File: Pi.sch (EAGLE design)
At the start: 11 parts, among them X1 RASPI_GPIO_B+#_BOX, X2 HDD, 5V 700mA, X3 MAC64L

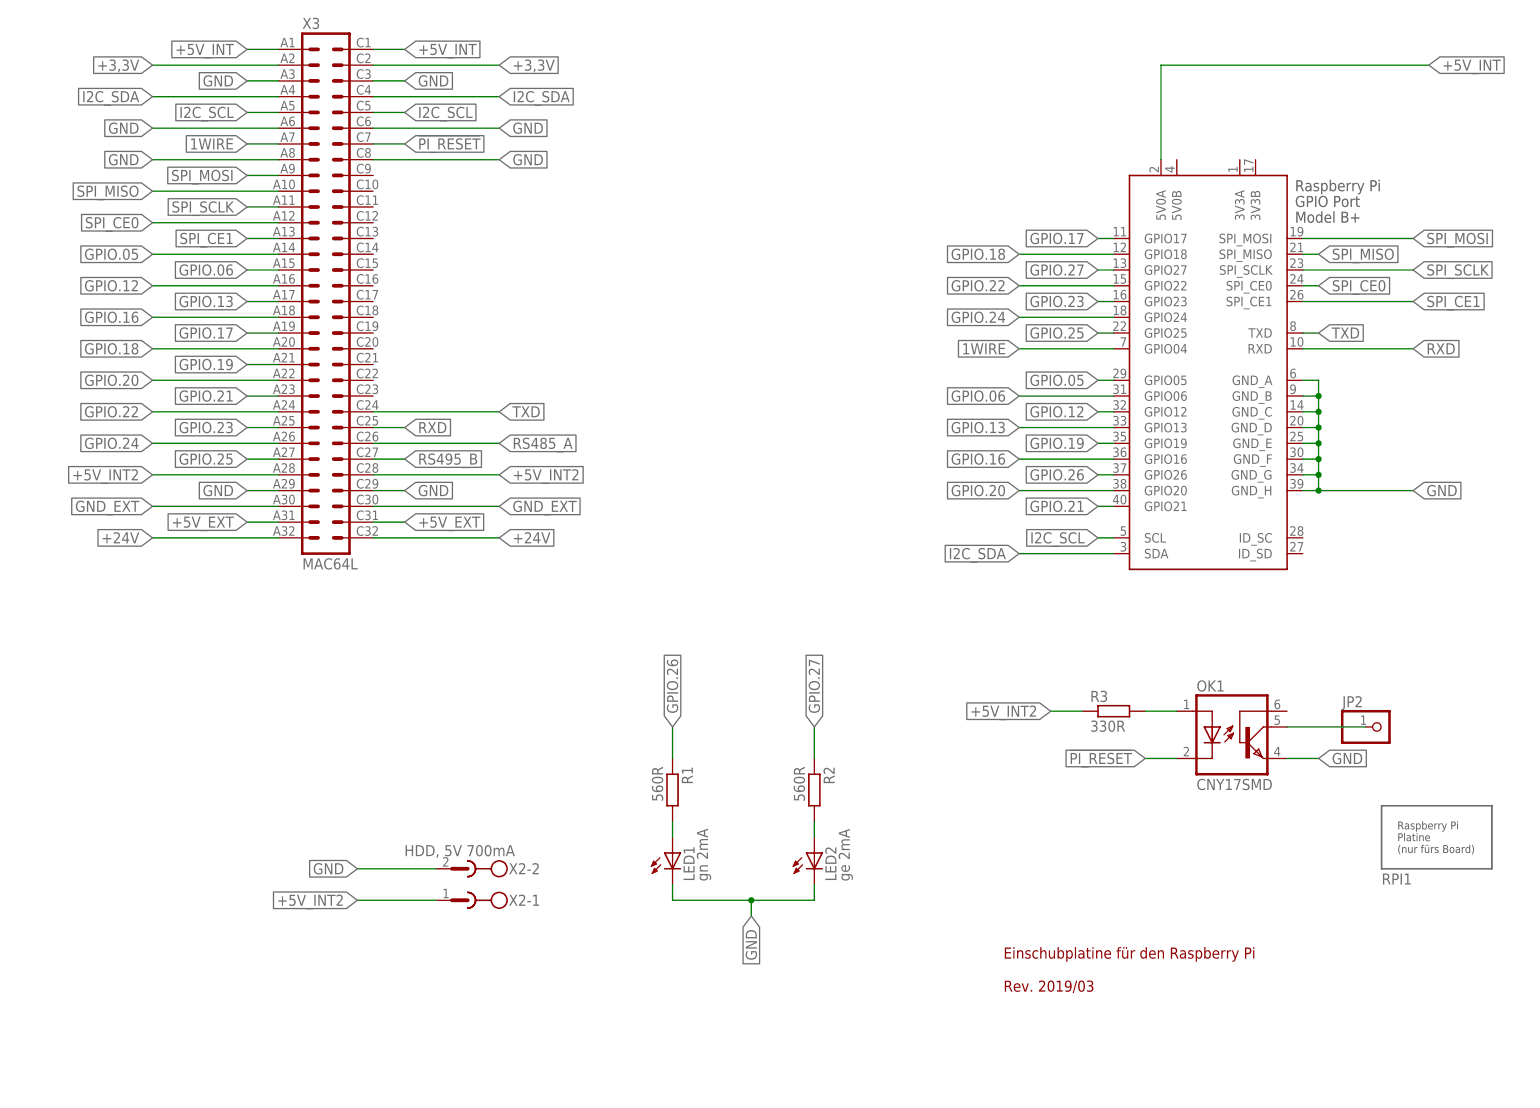
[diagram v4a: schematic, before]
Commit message: 1-Wire Sensor auf Raspi-Platine
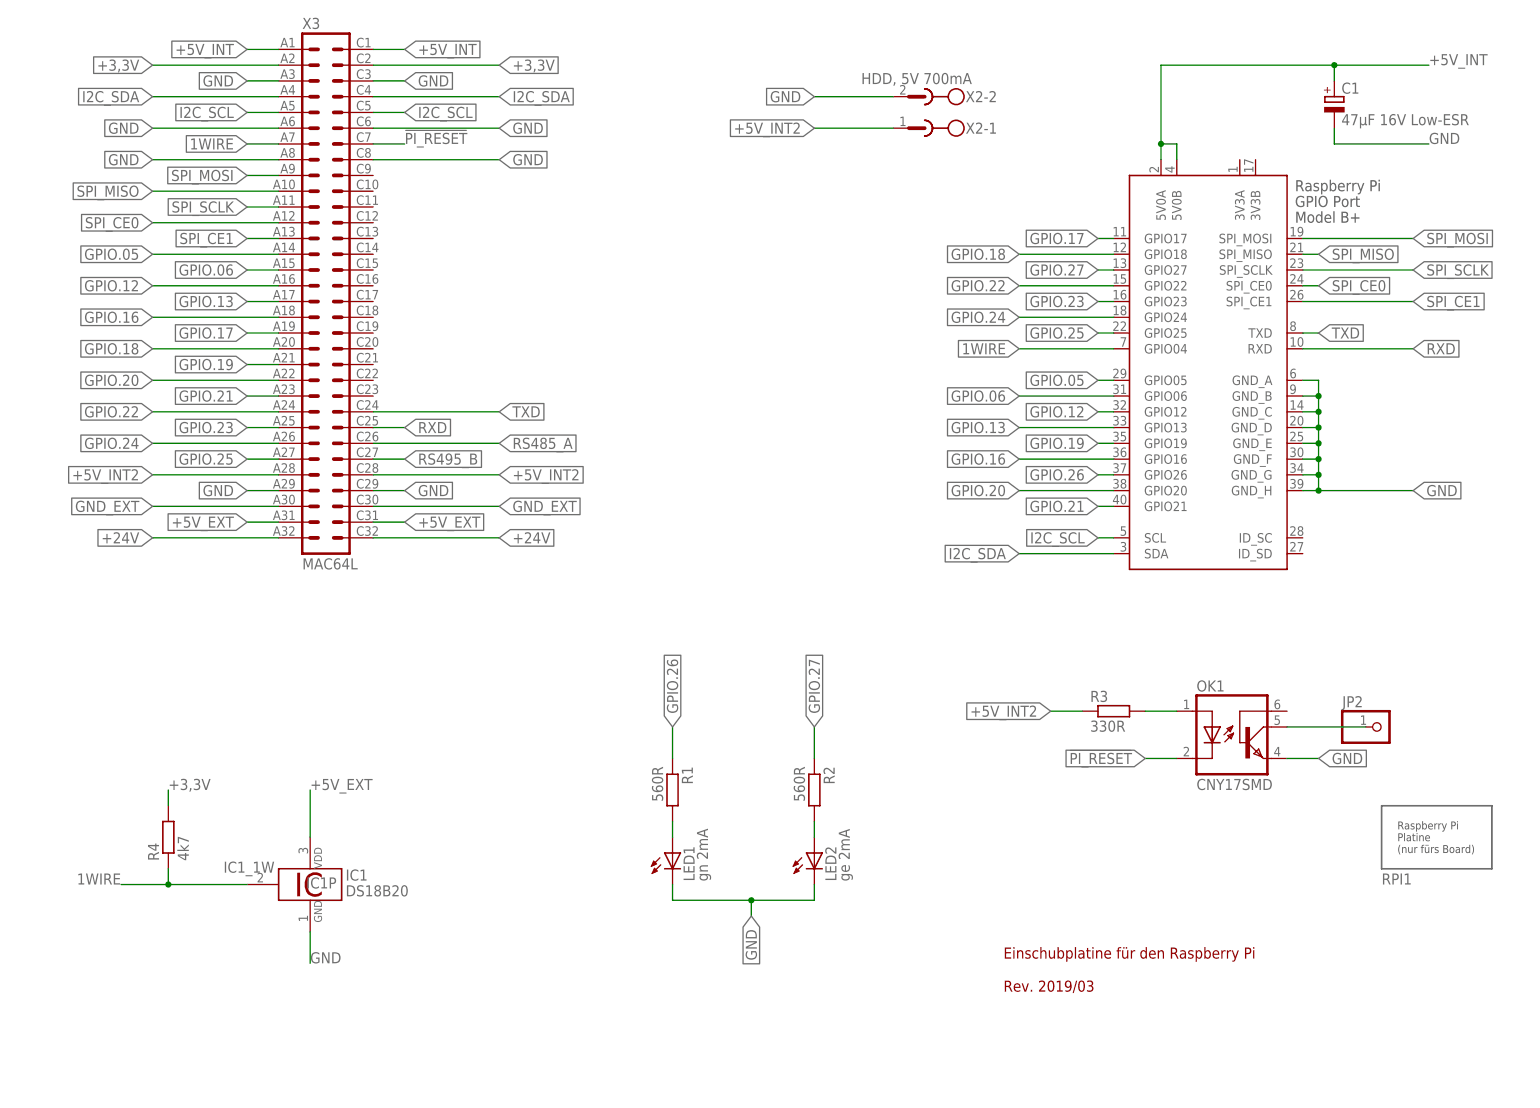
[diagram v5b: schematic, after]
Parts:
- added C1: 47µF 16V Low-ESR, rcl:CPOL-EUE2-5
- added IC1: DS18B20, 1wire:DS18B20
- added R4: 4k7, rcl:R-EU_0204/7
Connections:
- net +3,3V: now also R4.2
- net +5V_EXT: now also IC1P.VDD
- net +5V_INT: now also C1.+, X1.5V0B
- net 1WIRE: now also IC1_1W.1W, R4.1
- net GND: now also C1.-, IC1P.GND
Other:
- moved on the sheet: X2-1, X2-2
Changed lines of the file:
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@@
 <layer number="48" name="Document" color="7" fill="1" visible="no" active="no"/>
 <layer number="49" name="Reference" color="7" fill="1" visible="no" active="no"/>
+<layer number="50" name="dxf" color="7" fill="1" visible="no" active="no"/>
 <layer number="51" name="tDocu" color="7" fill="1" visible="no" active="no"/>
 <layer number="52" name="bDocu" color="7" fill="1" visible="no" active="no"/>
@@
 <layer number="98" name="Guide" color="6" fill="1" visible="yes" active="yes"/>
 <layer number="99" name="SpiceOrder" color="5" fill="1" visible="yes" active="yes"/>
+<layer number="250" name="Descript" color="3" fill="1" visible="no" active="no"/>
+<layer number="251" name="SMDround" color="12" fill="11" visible="no" active="no"/>
 </layers>
 <schematic xreflabel="%F%N/%S.%C%R" xrefpart="/%S.%C%R">
@@
 <part name="OK1" library="homepi" deviceset="CNY17" device="SMD"/>
 <part name="R3" library="rcl" deviceset="R-EU_" device="0204/5" value="330R"/>
+<part name="C1" library="rcl" deviceset="CPOL-EU" device="E2-5" value="47µF 16V Low-ESR"/>
+<part name="IC1" library="1wire" deviceset="DS18B20" device=""/>
+<part name="R4" library="rcl" deviceset="R-EU_" device="0204/7" value="4k7"/>
 </parts>
 <sheets>
@@
 <instance part="R2" gate="G$1" x="132.08" y="45.72" rot="R270"/>
 <instance part="LED2" gate="G$1" x="132.08" y="35.56"/>
-<instance part="X2" gate="-1" x="76.2" y="27.94" rot="R180"/>
-<instance part="X2" gate="-2" x="76.2" y="33.02" rot="R180"/>
+<instance part="X2" gate="-1" x="149.86" y="152.4" rot="R180"/>
+<instance part="X2" gate="-2" x="149.86" y="157.48" rot="R180"/>
 <instance part="X3" gate="G$1" x="53.34" y="127"/>
 <instance part="JP2" gate="G$1" x="223.52" y="55.88"/>
@@
 <instance part="OK1" gate="G$1" x="200.66" y="55.88"/>
 <instance part="R3" gate="G$1" x="180.34" y="58.42"/>
+<instance part="C1" gate="G$1" x="215.9" y="157.48"/>
+<instance part="IC1" gate="A" x="50.8" y="30.48"/>
+<instance part="IC1" gate="P" x="50.8" y="30.48"/>
+<instance part="IC1" gate="_1W" x="45.72" y="30.48"/>
+<instance part="R4" gate="G$1" x="27.94" y="38.1" rot="R90"/>
 </instances>
 <busses>
@@
 <label x="40.64" y="149.86" size="1.778" layer="95" rot="R180" xref="yes"/>
 </segment>
+<segment>
+<pinref part="IC1" gate="_1W" pin="1W"/>
+<wire x1="40.64" y1="30.48" x2="27.94" y2="30.48" width="0.1524" layer="91"/>
+<label x="20.32" y="30.48" size="1.778" layer="95" rot="MR0"/>
+<pinref part="R4" gate="G$1" pin="1"/>
+<wire x1="27.94" y1="30.48" x2="20.32" y2="30.48" width="0.1524" layer="91"/>
+<wire x1="27.94" y1="30.48" x2="27.94" y2="33.02" width="0.1524" layer="91"/>
+<junction x="27.94" y="30.48"/>
+</segment>
 </net>
 <net name="SPI_MOSI" class="0">
@@
 <label x="81.28" y="162.56" size="1.778" layer="95" xref="yes"/>
 </segment>
+<segment>
+<pinref part="R4" gate="G$1" pin="2"/>
+<wire x1="27.94" y1="43.18" x2="27.94" y2="45.72" width="0.1524" layer="91"/>
+<label x="27.94" y="45.72" size="1.778" layer="95"/>
+</segment>
 </net>
 <net name="N$15" class="0">
@@
 <segment>
 <pinref part="X2" gate="-1" pin="1"/>
-<wire x1="58.42" y1="27.94" x2="71.12" y2="27.94" width="0.1524" layer="91"/>
-<label x="58.42" y="27.94" size="1.778" layer="95" rot="R180" xref="yes"/>
+<wire x1="132.08" y1="152.4" x2="144.78" y2="152.4" width="0.1524" layer="91"/>
+<label x="132.08" y="152.4" size="1.778" layer="95" rot="R180" xref="yes"/>
 </segment>
 <segment>
@@
 <segment>
 <pinref part="X1" gate="G$1" pin="5V0A"/>
-<wire x1="187.96" y1="147.32" x2="187.96" y2="162.56" width="0.1524" layer="91"/>
-<wire x1="187.96" y1="162.56" x2="231.14" y2="162.56" width="0.1524" layer="91"/>
-<label x="231.14" y="162.56" size="1.778" layer="95" xref="yes"/>
+<wire x1="187.96" y1="147.32" x2="187.96" y2="149.86" width="0.1524" layer="91"/>
+<wire x1="187.96" y1="149.86" x2="187.96" y2="162.56" width="0.1524" layer="91"/>
+<wire x1="187.96" y1="162.56" x2="215.9" y2="162.56" width="0.1524" layer="91"/>
+<label x="231.14" y="162.56" size="1.778" layer="95"/>
+<pinref part="C1" gate="G$1" pin="+"/>
+<wire x1="215.9" y1="162.56" x2="231.14" y2="162.56" width="0.1524" layer="91"/>
+<wire x1="215.9" y1="160.02" x2="215.9" y2="162.56" width="0.1524" layer="91"/>
+<junction x="215.9" y="162.56"/>
+<pinref part="X1" gate="G$1" pin="5V0B"/>
+<wire x1="187.96" y1="149.86" x2="190.5" y2="149.86" width="0.1524" layer="91"/>
+<wire x1="190.5" y1="149.86" x2="190.5" y2="147.32" width="0.1524" layer="91"/>
+<junction x="187.96" y="149.86"/>
 </segment>
 <segment>
@@
 <label x="66.04" y="88.9" size="1.778" layer="95" xref="yes"/>
 </segment>
+<segment>
+<pinref part="IC1" gate="P" pin="VDD"/>
+<wire x1="50.8" y1="45.72" x2="50.8" y2="38.1" width="0.1524" layer="91"/>
+<label x="50.8" y="45.72" size="1.778" layer="95"/>
+</segment>
 </net>
 <net name="+24V" class="0">
@@
 <segment>
 <pinref part="X2" gate="-2" pin="1"/>
-<wire x1="58.42" y1="33.02" x2="71.12" y2="33.02" width="0.1524" layer="91"/>
-<label x="58.42" y="33.02" size="1.778" layer="95" rot="R180" xref="yes"/>
+<wire x1="132.08" y1="157.48" x2="144.78" y2="157.48" width="0.1524" layer="91"/>
+<label x="132.08" y="157.48" size="1.778" layer="95" rot="R180" xref="yes"/>
 </segment>
 <segment>
@@
 <label x="213.36" y="50.8" size="1.778" layer="95" xref="yes"/>
 </segment>
+<segment>
+<pinref part="C1" gate="G$1" pin="-"/>
+<wire x1="215.9" y1="152.4" x2="215.9" y2="149.86" width="0.1524" layer="91"/>
+<wire x1="215.9" y1="149.86" x2="231.14" y2="149.86" width="0.1524" layer="91"/>
+<label x="231.14" y="149.86" size="1.778" layer="95"/>
+</segment>
+<segment>
+<pinref part="IC1" gate="P" pin="GND"/>
+<wire x1="50.8" y1="22.86" x2="50.8" y2="17.78" width="0.1524" layer="91"/>
+<label x="50.8" y="17.78" size="1.778" layer="95"/>
+</segment>
 </net>
 <net name="N$2" class="0">
@@
 <pinref part="X3" gate="G$1" pin="C7"/>
 <wire x1="60.96" y1="149.86" x2="66.04" y2="149.86" width="0.1524" layer="91"/>
-<label x="66.04" y="149.86" size="1.778" layer="95" xref="yes"/>
-</segment>
-</net>
+<label x="66.04" y="149.86" size="1.778" layer="95"/>
+</segment>
+</net>

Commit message: Diverse Anpassungen
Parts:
- X1: value RASPI_GPIO_B+#_BOX -> RASPI_GPIO_B+#_PIN; device raspberrypi_bastelstube_v13:RASPI_GPIO_B+#_BOX -> raspberrypi_bastelstube_v13:RASPI_GPIO_B+#_PIN
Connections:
- net RS485_A renamed CANL
- net RS495_B renamed CANH

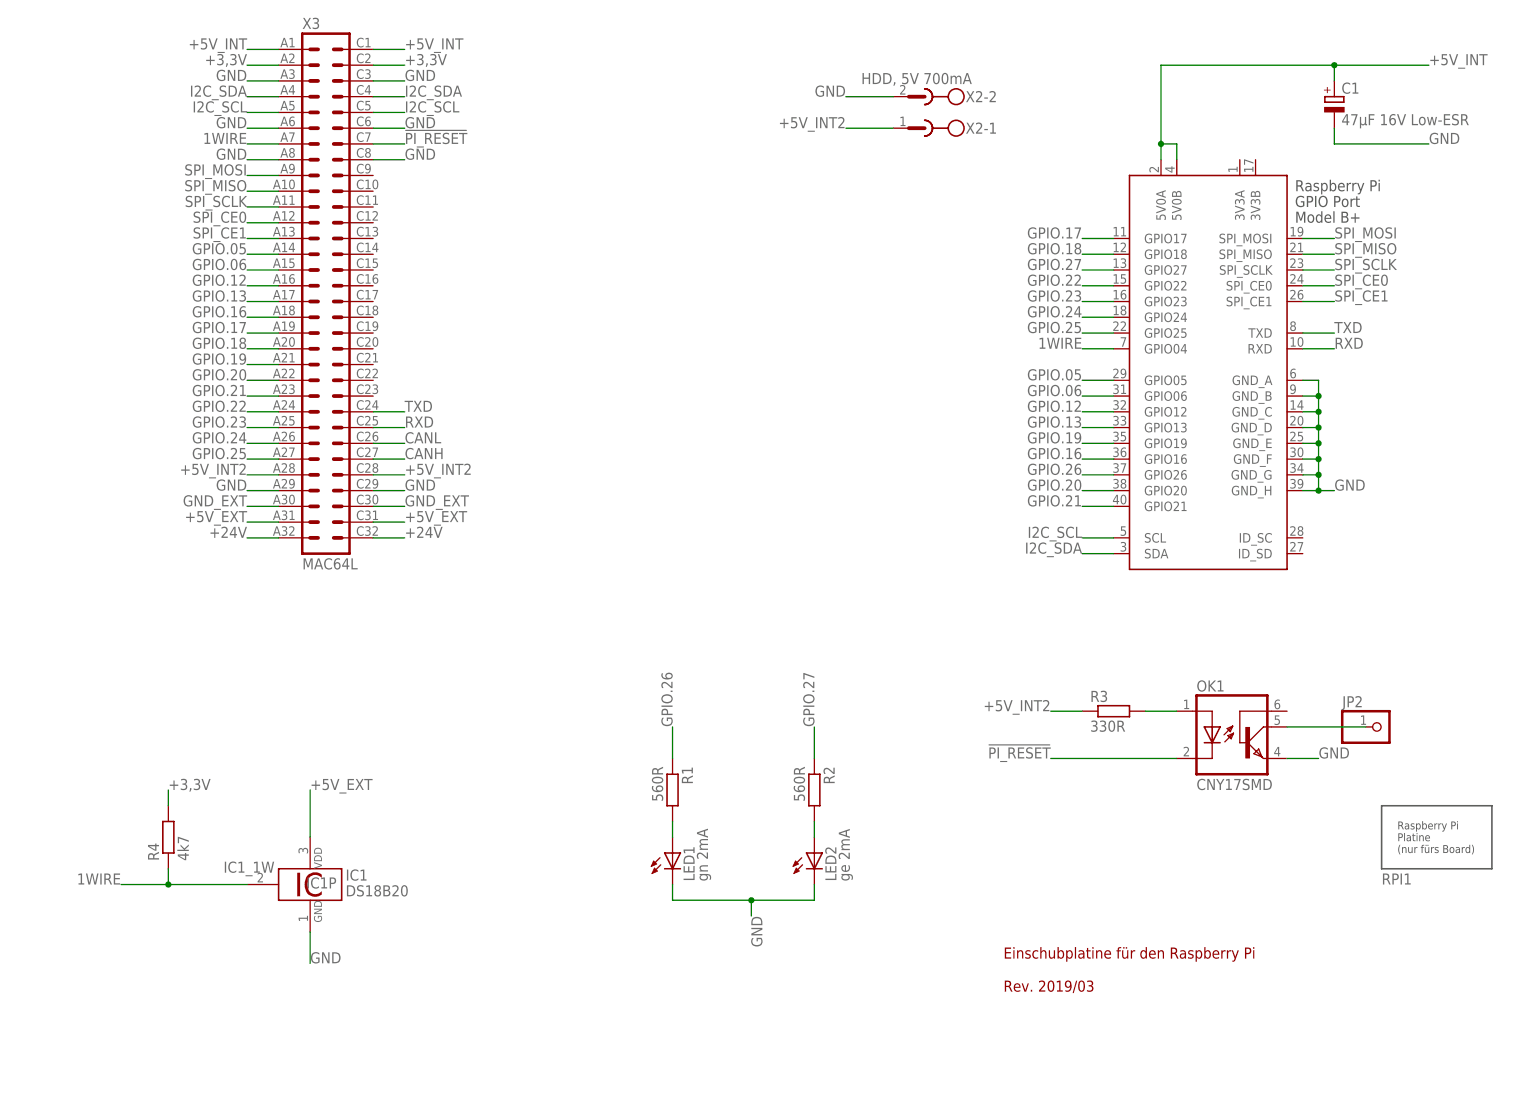
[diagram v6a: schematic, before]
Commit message: Pi, CanBus, Stromversorgung, Steckverbinder angepasst
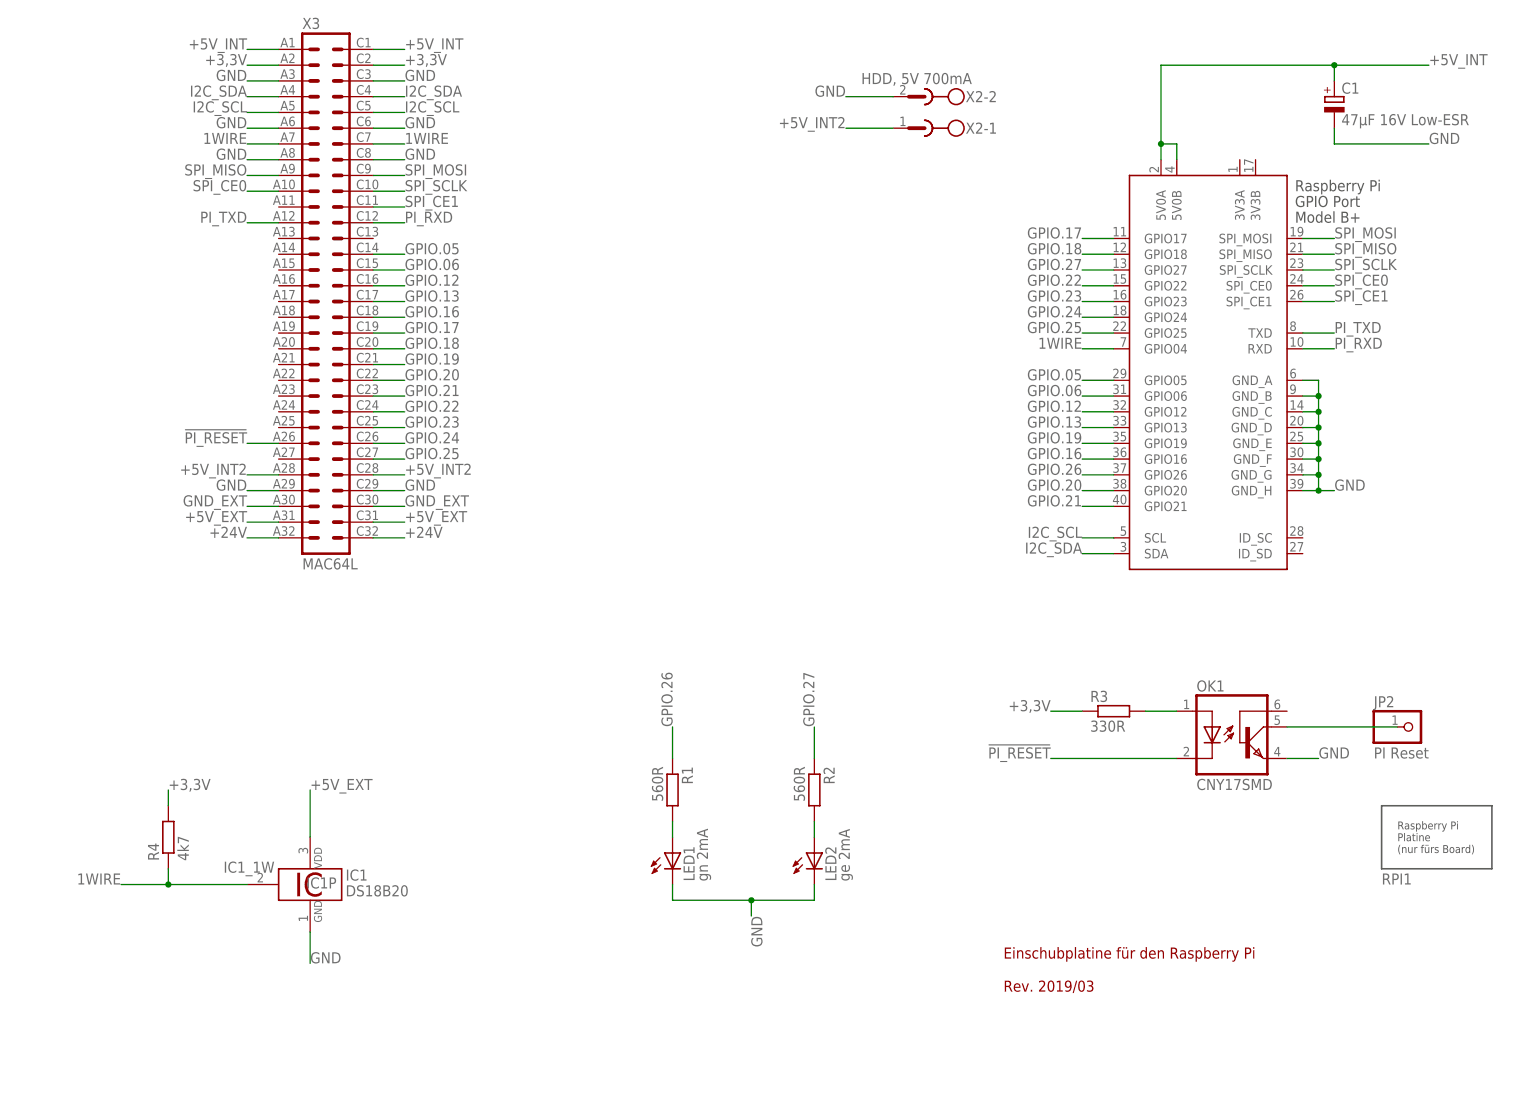
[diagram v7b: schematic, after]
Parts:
- JP2: value (none) -> PI Reset
- R1, R2, R4: device rcl:R-EU_0204/7 -> rcl:R-EU_R1206
- R3: device rcl:R-EU_0204/5 -> rcl:R-EU_R1206
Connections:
- removed net CANH: X3.C27
- removed net CANL: X3.C26
- removed net RXD: X1.RXD, X3.C25
- removed net TXD: X1.TXD, X3.C24
- new net PI_RXD: X1.RXD, X3.C12
- new net PI_TXD: X1.TXD, X3.A12
- net !PI_RESET: now also X3.A26; no longer X3.C7
- net +3,3V: now also R3.1
- net +5V_INT2: no longer R3.1
- net 1WIRE: now also X3.C7
- net GPIO.05: now also X3.C14; no longer X3.A14
- net GPIO.06: now also X3.C15; no longer X3.A15
- net GPIO.12: now also X3.C16; no longer X3.A16
- net GPIO.13: now also X3.C17; no longer X3.A17
- net GPIO.16: now also X3.C18; no longer X3.A18
- net GPIO.17: now also X3.C19; no longer X3.A19
- net GPIO.18: now also X3.C20; no longer X3.A20
- net GPIO.19: now also X3.C21; no longer X3.A21
- net GPIO.20: now also X3.C22; no longer X3.A22
- net GPIO.21: now also X3.C23; no longer X3.A23
- net GPIO.22: now also X3.C24; no longer X3.A24
- net GPIO.23: now also X3.C25; no longer X3.A25
- net GPIO.24: now also X3.C26; no longer X3.A26
- net GPIO.25: now also X3.C27; no longer X3.A27
- net SPI_CE0: now also X3.A10; no longer X3.A12
- net SPI_CE1: now also X3.C11; no longer X3.A13
- net SPI_MISO: now also X3.A9; no longer X3.A10
- net SPI_MOSI: now also X3.C9; no longer X3.A9
- net SPI_SCLK: now also X3.C10; no longer X3.A11
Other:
- moved on the sheet: JP2
